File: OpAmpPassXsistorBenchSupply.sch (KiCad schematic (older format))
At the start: 0 parts

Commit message: pulling in libraries and modules.  setting up input jacks and positive and negative supply rails.
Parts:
- added C? (x2): C_CER, ~, symbol C_CER
- added C? (x4): C_EL, ~, symbol C_EL
- added CON? (x3): BARREL_JACK, ~, symbol BARREL_JACK
- added D? (x4): DIODE, ~, symbol DIODE
- added R? (x4): R_0W25_1PCT, ~, symbol R_0W25_1PCT
- added U? (x2): LM324N, symbol LM324N
- added U?: LM317, ~, symbol LM317
- added U?: LM337, ~, symbol LM337
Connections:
- net labels added: GND, Vin+_raw, Vin-_raw
- wire segments 0 -> 56
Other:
- note added: "negative supply"
- note added: "positive supply"

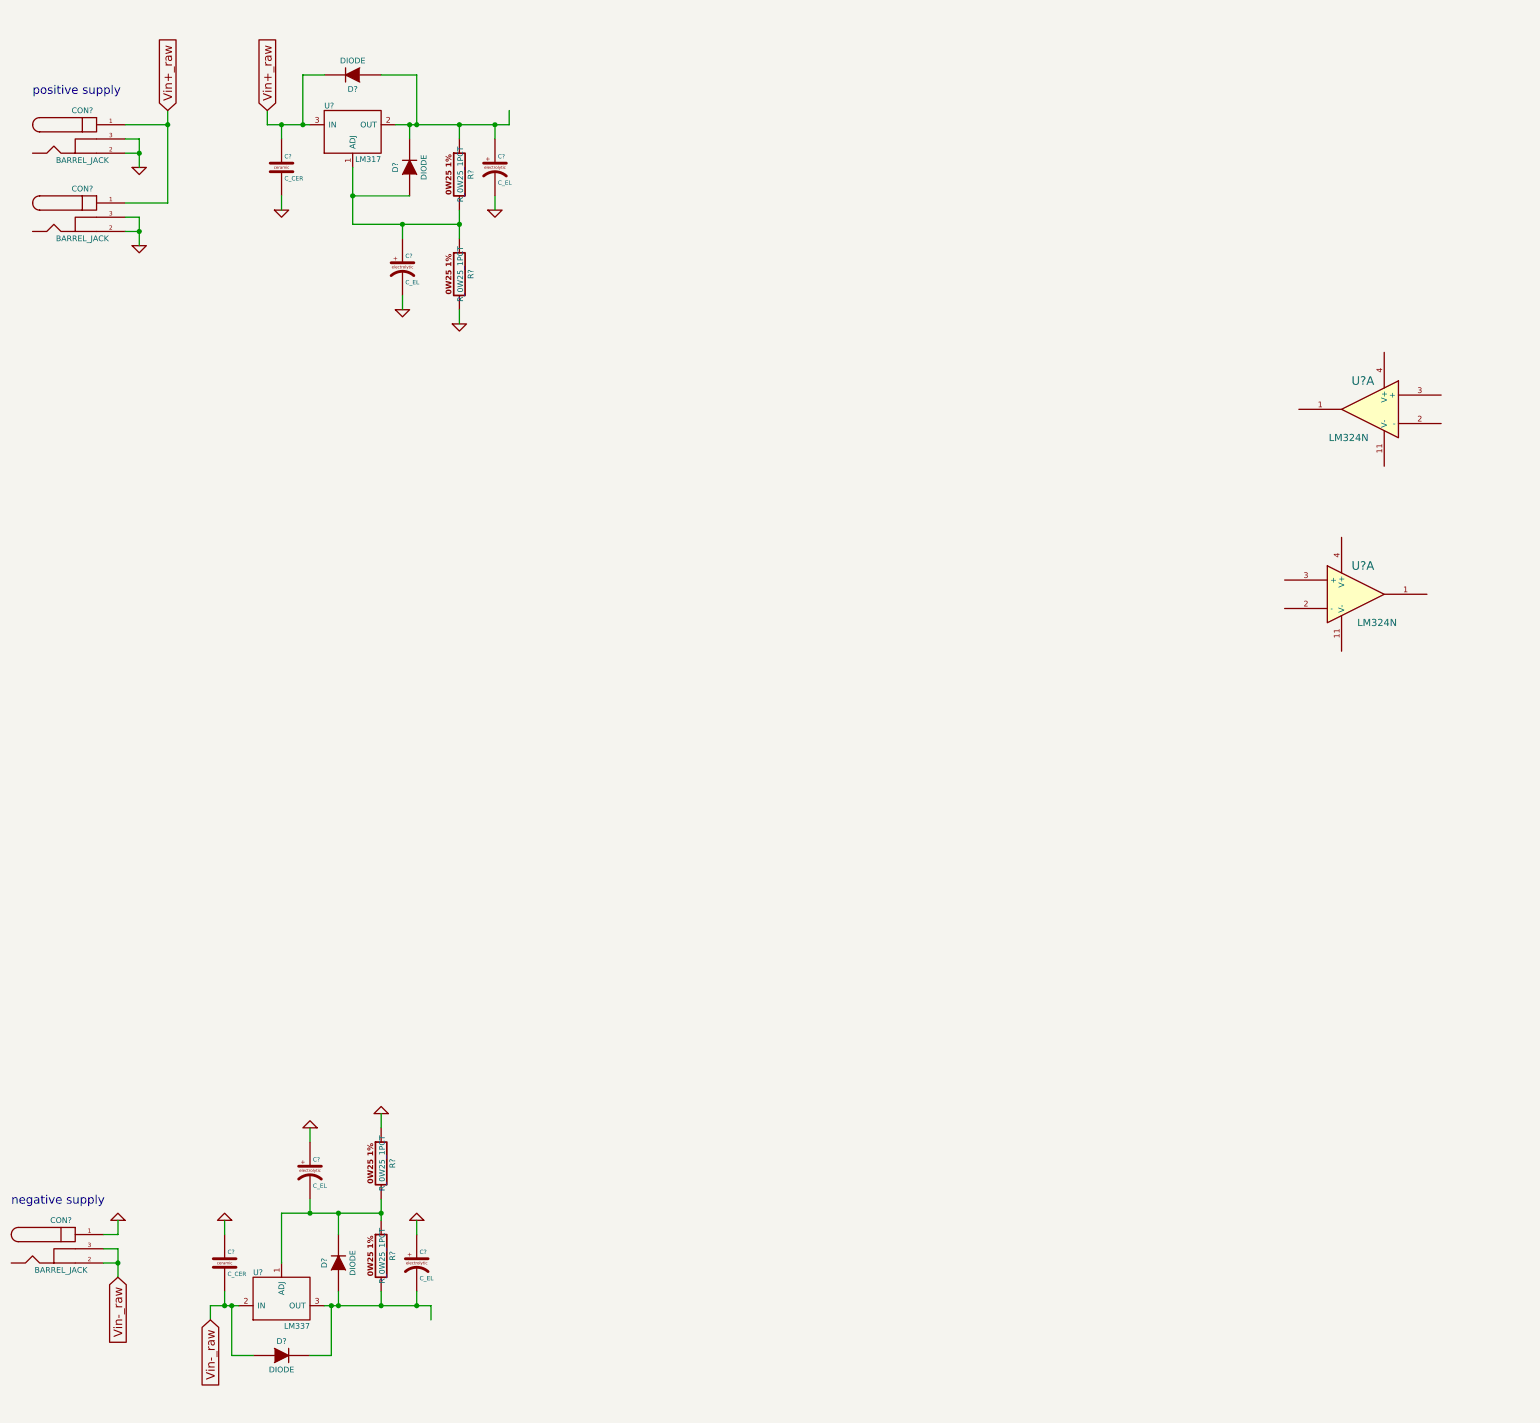
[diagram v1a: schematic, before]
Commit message: implementing basic voltage control schematic
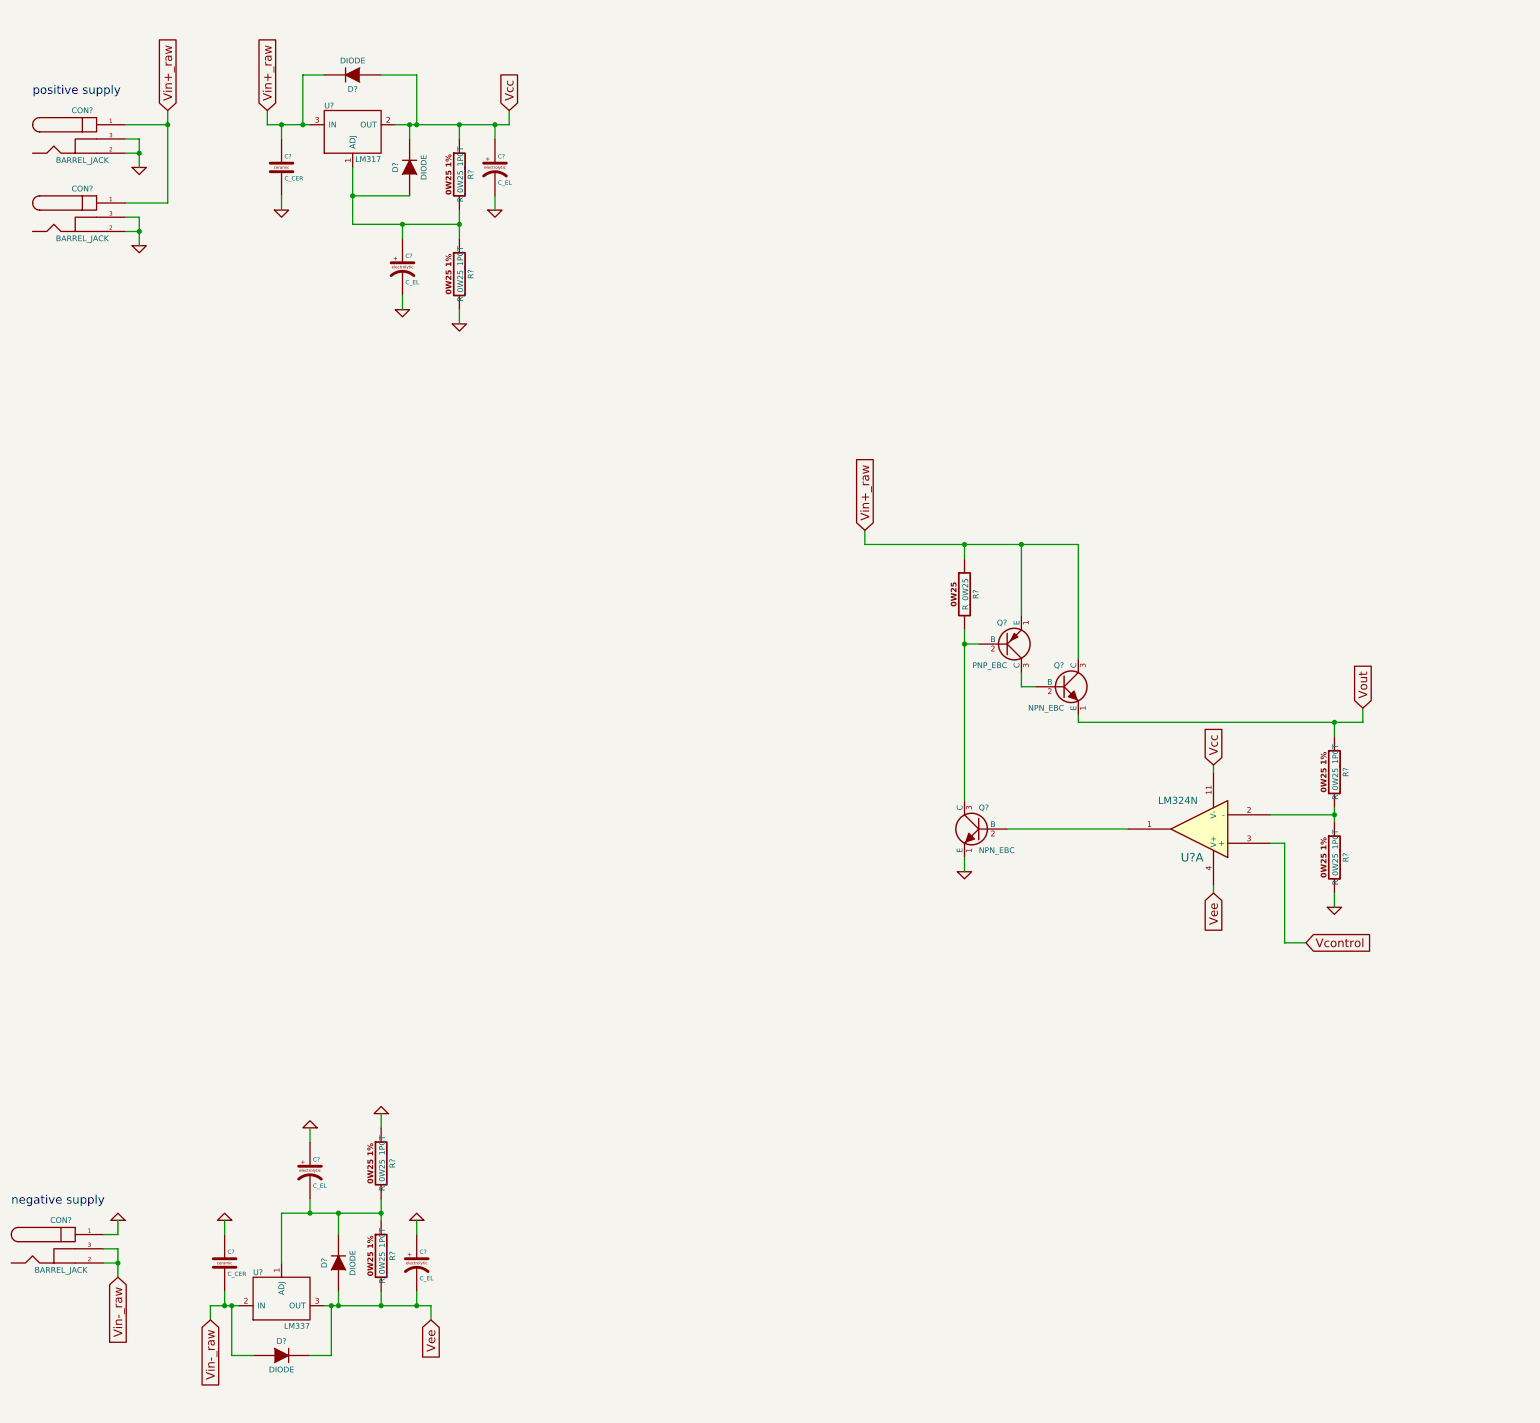
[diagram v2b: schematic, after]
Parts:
- removed U?: LM324N, symbol LM324N
- added Q? (x2): NPN_EBC, ~, symbol NPN_EBC
- added Q?: PNP_EBC, ~, symbol PNP_EBC
- added R? (x2): R_0W25_1PCT, ~, symbol R_0W25_1PCT
- added R?: R_0W25, ~, symbol R_0W25
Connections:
- net labels added: Vcc, Vcontrol, Vee, Vout
- wire segments 56 -> 79
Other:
- moved on the sheet: U?A
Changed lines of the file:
@@
 EESchema Schematic File Version 2
+LIBS:transistors_PL
 LIBS:diodes_PL
 LIBS:resistors_PL
@@
 L LM324N U?
 U 1 1 533648D0
-P 10350 3400
-F 0 "U?" H 10400 3600 60  0000 C CNN
-F 1 "LM324N" H 10500 3200 50  0000 C CNN
-F 2 "" H 10350 3400 60  0000 C CNN
-F 3 "" H 10350 3400 60  0000 C CNN
-	1    10350 3400
-	-1   0    0    -1
-$EndComp
-$Comp
-L LM324N U?
-U 1 1 5336492C
-P 10250 4700
-F 0 "U?" H 10300 4900 60  0000 C CNN
-F 1 "LM324N" H 10400 4500 50  0000 C CNN
-F 2 "" H 10250 4700 60  0000 C CNN
-F 3 "" H 10250 4700 60  0000 C CNN
-	1    10250 4700
-	1    0    0    -1
+P 9150 6350
+F 0 "U?" H 9200 6550 60  0000 C CNN
+F 1 "LM324N" H 9300 6150 50  0000 C CNN
+F 2 "" H 9150 6350 60  0000 C CNN
+F 3 "" H 9150 6350 60  0000 C CNN
+	1    9150 6350
+	-1   0    0    1
 $EndComp
 $Comp
@@
 	3750 9700 3750 9800
 Connection ~ 3650 9700
+$Comp
+L NPN_EBC Q?
+U 1 1 533659BB
+P 8200 5350
+F 0 "Q?" H 8200 5500 40  0000 R CNN
+F 1 "NPN_EBC" H 8200 5200 40  0000 R CNN
+F 2 "~" H 8200 5350 60  0000 C CNN
+F 3 "~" H 8200 5350 60  0000 C CNN
+	1    8200 5350
+	1    0    0    -1
+$EndComp
+$Comp
+L R_0W25_1PCT R?
+U 1 1 53365A71
+P 10100 5950
+F 0 "R?" V 10180 5950 40  0000 C CNN
+F 1 "R_0W25_1PCT" V 10107 5951 40  0000 C CNN
+F 2 "~" V 10030 5950 30  0000 C CNN
+F 3 "~" H 10100 5950 30  0000 C CNN
+	1    10100 5950
+	1    0    0    -1
+$EndComp
+$Comp
+L R_0W25_1PCT R?
+U 1 1 53365A7E
+P 10100 6550
+F 0 "R?" V 10180 6550 40  0000 C CNN
+F 1 "R_0W25_1PCT" V 10107 6551 40  0000 C CNN
+F 2 "~" V 10030 6550 30  0000 C CNN
+F 3 "~" H 10100 6550 30  0000 C CNN
+	1    10100 6550
+	1    0    0    -1
+$EndComp
+Wire Wire Line
+	10100 5700 10100 5600
+Connection ~ 10100 5600
+Wire Wire Line
+	10100 6300 10100 6200
+Wire Wire Line
+	9650 6250 10100 6250
+Connection ~ 10100 6250
+$Comp
+L GND #PWR?
+U 1 1 53365B9F
+P 10100 6900
+F 0 "#PWR?" H 10100 6900 30  0001 C CNN
+F 1 "GND" H 10100 6830 30  0001 C CNN
+F 2 "" H 10100 6900 60  0000 C CNN
+F 3 "" H 10100 6900 60  0000 C CNN
+	1    10100 6900
+	1    0    0    -1
+$EndComp
+Wire Wire Line
+	10100 6800 10100 6900
+Wire Wire Line
+	7800 6350 8650 6350
+Wire Wire Line
+	8300 4350 8300 5150
+Wire Wire Line
+	8000 5350 7900 5350
+Wire Wire Line
+	8300 5550 8300 5600
+$Comp
+L PNP_EBC Q?
+U 1 1 53365E81
+P 7800 5050
+F 0 "Q?" H 7800 5200 40  0000 R CNN
+F 1 "PNP_EBC" H 7800 4900 40  0000 R CNN
+F 2 "~" H 7800 5050 60  0000 C CNN
+F 3 "~" H 7800 5050 60  0000 C CNN
+	1    7800 5050
+	1    0    0    -1
+$EndComp
+Wire Wire Line
+	7900 5350 7900 5250
+Wire Wire Line
+	7900 4350 7900 4850
+Wire Wire Line
+	7600 5050 7500 5050
+$Comp
+L R_0W25 R?
+U 1 1 5336600F
+P 7500 4700
+F 0 "R?" V 7580 4700 40  0000 C CNN
+F 1 "R_0W25" V 7507 4701 40  0000 C CNN
+F 2 "~" V 7430 4700 30  0000 C CNN
+F 3 "~" H 7500 4700 30  0000 C CNN
+	1    7500 4700
+	1    0    0    -1
+$EndComp
+Wire Wire Line
+	7500 4950 7500 6150
+Wire Wire Line
+	6800 4350 8300 4350
+Connection ~ 7900 4350
+Wire Wire Line
+	7500 4450 7500 4350
+Connection ~ 7500 4350
+$Comp
+L NPN_EBC Q?
+U 1 1 533661A0
+P 7600 6350
+F 0 "Q?" H 7600 6500 40  0000 R CNN
+F 1 "NPN_EBC" H 7600 6200 40  0000 R CNN
+F 2 "~" H 7600 6350 60  0000 C CNN
+F 3 "~" H 7600 6350 60  0000 C CNN
+	1    7600 6350
+	-1   0    0    -1
+$EndComp
+Connection ~ 7500 5050
+$Comp
+L GND #PWR?
+U 1 1 5336627C
+P 7500 6650
+F 0 "#PWR?" H 7500 6650 30  0001 C CNN
+F 1 "GND" H 7500 6580 30  0001 C CNN
+F 2 "" H 7500 6650 60  0000 C CNN
+F 3 "" H 7500 6650 60  0000 C CNN
+	1    7500 6650
+	1    0    0    -1
+$EndComp
+Wire Wire Line
+	7500 6550 7500 6650
+Wire Wire Line
+	8300 5600 10300 5600
+Text GLabel 6800 4250 1    60   Input ~ 0
+Vin+_raw
+Wire Wire Line
+	6800 4350 6800 4250
+Text GLabel 4300 1300 1    60   Input ~ 0
+Vcc
+Text GLabel 3750 9800 3    60   Input ~ 0
+Vee
+Text GLabel 9250 5900 1    60   Input ~ 0
+Vcc
+Wire Wire Line
+	9250 5950 9250 5900
+Text GLabel 9250 6800 3    60   Input ~ 0
+Vee
+Wire Wire Line
+	9250 6750 9250 6800
+Text GLabel 10300 5500 1    60   Input ~ 0
+Vout
+Wire Wire Line
+	10300 5600 10300 5500
+Text GLabel 9900 7150 2    60   Input ~ 0
+Vcontrol
+Wire Wire Line
+	9650 6450 9750 6450
+Wire Wire Line
+	9750 6450 9750 7150
+Wire Wire Line
+	9750 7150 9900 7150
 $EndSCHEMATC

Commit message: adding basic current and power control stubs
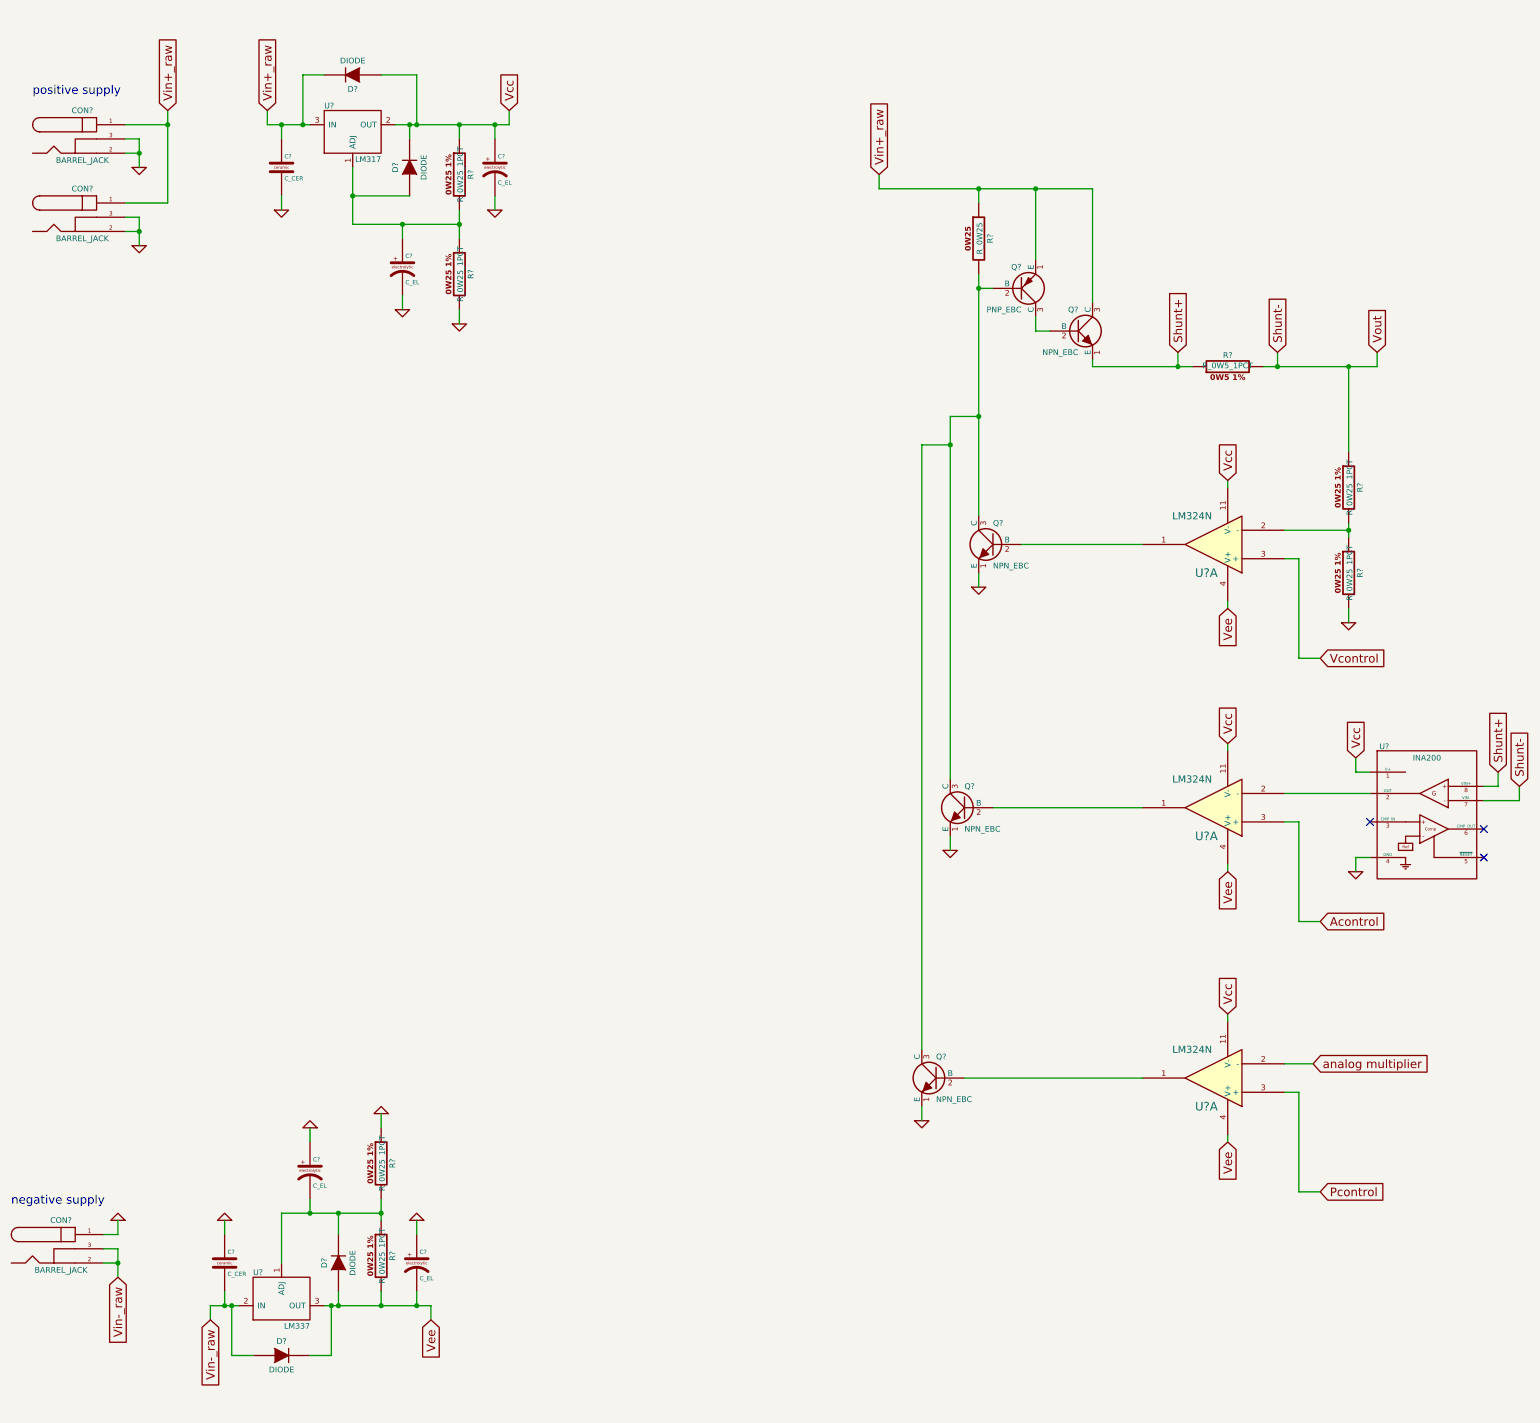
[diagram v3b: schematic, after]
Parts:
- added Q? (x2): NPN_EBC, ~, symbol NPN_EBC
- added R?: R_0W5_1PCT, ~, symbol R_0W5_1PCT
- added U?: INA200, ~, symbol INA200
- added U? (x2): LM324N, symbol LM324N
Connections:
- net GND: now also Q?.1 (E), Q?.1 (E), U?.4 (GND)
- net Vcc: now also U?.1 (V+), U?.11 (V-), U?.11 (V-)
- net Vee: now also U?.4 (V+), U?.4 (V+)
- net at Q?.2 (B), Q?.3 (C), R?.2: now also Q?.3 (C), Q?.3 (C)
- net Vout renamed Shunt+
- net Shunt+: now also R?.1, U?.8 (VIN+); no longer R?.1
- new net: U?.2 (-), U?.2 (OUT)
- new net: Q?.2 (B), U?.1 (x2)
- new net Acontrol: U?.3 (+)
- new net Pcontrol: U?.3 (+)
- new net Shunt-: R?.1, R?.2, U?.7 (VIN-)
- new net analog multiplier: U?.2 (-)
- no-connect marks 0 -> 3
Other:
- moved on the sheet: Q?, R?, U?A
